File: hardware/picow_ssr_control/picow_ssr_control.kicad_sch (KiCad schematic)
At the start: 6 parts

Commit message: Updated schemas
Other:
- sheet Pico W Control ports: added none; removed VBUS, VSYS
- sheet Power Management ports: added none; removed VBUS, VSYS
- note added: "Pico W SSR Control"
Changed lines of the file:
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@@
   (title_block
     (title "Picow SSR Control")
-    (date "2023-01-27")
+    (date "2023-01-28")
     (rev "0.0.10")
     (comment 2 "http://creativecommons.org/licenses/by-sa/4.0/")
@@
     (comment 6 "Hardware License: CERN-OHL-W")
   )
-  (junction (at 127 55.88) (diameter 0) (color 255 255 0 1)
+  (junction (at 111.76 40.64) (diameter 0) (color 255 255 0 1)
   )
   (junction (at 27.94 152.4) (diameter 0) (color 0 0 0 0)
@@
   (junction (at 27.94 157.48) (diameter 0) (color 0 0 0 0)
   )
-  (junction (at 132.08 71.12) (diameter 0) (color 255 255 0 1)
+  (junction (at 116.84 55.88) (diameter 0) (color 255 255 0 1)
   )
   (polyline (pts (xy 17.78 172.72) (xy 17.78 195.58))
@@
     (stroke (width 0) (type default) (color 0 0 0 0))
   )
-  (bus (pts (xy 127 55.88) (xy 127 106.68))
+  (bus (pts (xy 111.76 40.64) (xy 111.76 81.28))
     (stroke (width 0) (type default) (color 255 255 0 1))
   )
@@
     (stroke (width 0) (type default) (color 0 0 0 0))
   )
-  (bus (pts (xy 132.08 71.12) (xy 152.4 71.12))
+  (bus (pts (xy 116.84 55.88) (xy 132.08 55.88))
     (stroke (width 0) (type default) (color 255 255 0 1))
   )
@@
     (stroke (width 0) (type default) (color 0 0 0 0))
   )
-  (bus (pts (xy 127 55.88) (xy 152.4 55.88))
+  (bus (pts (xy 111.76 40.64) (xy 132.08 40.64))
     (stroke (width 0) (type default) (color 255 255 0 1))
   )
@@
     (stroke (width 0) (type default) (color 0 0 0 0))
   )
-  (bus (pts (xy 132.08 114.3) (xy 114.3 114.3))
+  (bus (pts (xy 116.84 88.9) (xy 99.06 88.9))
     (stroke (width 0) (type default) (color 255 255 0 1))
   )
@@
     (stroke (width 0) (type default) (color 0 0 0 0))
   )
-  (wire (pts (xy 45.72 55.88) (xy 76.2 55.88))
-    (stroke (width 0) (type default) (color 0 0 0 0))
-  )
   (wire (pts (xy 27.94 152.4) (xy 27.94 157.48))
     (stroke (width 0) (type default) (color 0 0 0 0))
   )
-  (bus (pts (xy 114.3 106.68) (xy 127 106.68))
+  (bus (pts (xy 99.06 81.28) (xy 111.76 81.28))
     (stroke (width 0) (type default) (color 255 255 0 1))
   )
@@
     (stroke (width 0) (type default) (color 0 0 0 0))
   )
-  (bus (pts (xy 132.08 71.12) (xy 132.08 114.3))
+  (bus (pts (xy 116.84 55.88) (xy 116.84 88.9))
     (stroke (width 0) (type default) (color 255 255 0 1))
   )
-  (bus (pts (xy 114.3 71.12) (xy 132.08 71.12))
+  (bus (pts (xy 99.06 55.88) (xy 116.84 55.88))
     (stroke (width 0) (type default) (color 255 255 0 1))
   )
-  (wire (pts (xy 45.72 60.96) (xy 76.2 60.96))
-    (stroke (width 0) (type default) (color 0 0 194 1))
-  )
-  (bus (pts (xy 114.3 55.88) (xy 127 55.88))
+  (bus (pts (xy 99.06 40.64) (xy 111.76 40.64))
     (stroke (width 0) (type default) (color 255 255 0 1))
   )
@@
     )
   )
+  (text "Pico W SSR Control" (at 15.24 20.32 0)
+    (effects (font (size 4 4) bold) (justify left bottom))
+  )
   (text "Mounting Holes" (at 20.32 142.24 0)
     (effects (font (size 2 2) (thickness 0.4) bold) (justify left bottom))
@@
     )
   )
-  (sheet (at 76.2 101.6) (size 38.1 17.78) (fields_autoplaced)
+  (sheet (at 60.96 76.2) (size 38.1 17.78) (fields_autoplaced)
     (stroke (width 0.1524) (type solid) (color 0 0 0 0))
     (fill (color 0 0 0 0.0000))
-    (property "Sheet name" "Manual Control" (id 0) (at 76.2 100.5234 0)
+    (property "Sheet name" "Manual Control" (id 0) (at 60.96 75.1234 0)
       (effects (font (size 2 2) bold) (justify left bottom))
     )
-    (property "Sheet file" "manual_control.kicad_sch" (id 1) (at 76.2 119.9646 0)
+    (property "Sheet file" "manual_control.kicad_sch" (id 1) (at 60.96 94.5646 0)
       (effects (font (size 1.27 1.27)) (justify left top))
     )
-    (pin "BANK_A{CNTL[1..4]}" passive (at 114.3 106.68 0)
+    (pin "BANK_A{CNTL[1..4]}" passive (at 99.06 81.28 0)
       (effects (font (size 1.27 1.27)) (justify right))
     )
-    (pin "BANK_B{CNTL[5..8]}" passive (at 114.3 114.3 0)
+    (pin "BANK_B{CNTL[5..8]}" passive (at 99.06 88.9 0)
       (effects (font (size 1.27 1.27)) (justify right))
     )
   )
-  (sheet (at 152.4 50.8) (size 38.1 25.4) (fields_autoplaced)
+  (sheet (at 132.08 35.56) (size 38.1 25.4) (fields_autoplaced)
     (stroke (width 0.1524) (type solid) (color 0 0 0 0))
     (fill (color 0 0 0 0.0000))
-    (property "Sheet name" "Control Out" (id 0) (at 152.4 49.7234 0)
+    (property "Sheet name" "Control Out" (id 0) (at 132.08 34.4834 0)
       (effects (font (size 2 2) bold) (justify left bottom))
     )
-    (property "Sheet file" "control_out.kicad_sch" (id 1) (at 152.4 76.7846 0)
+    (property "Sheet file" "control_out.kicad_sch" (id 1) (at 132.08 61.5446 0)
       (effects (font (size 1.27 1.27)) (justify left top))
     )
-    (pin "BANK_B{CNTL[5..8]}" input (at 152.4 71.12 180)
+    (pin "BANK_B{CNTL[5..8]}" input (at 132.08 55.88 180)
       (effects (font (size 1.27 1.27)) (justify left))
     )
-    (pin "BANK_A{CNTL[1..4]}" input (at 152.4 55.88 180)
+    (pin "BANK_A{CNTL[1..4]}" input (at 132.08 40.64 180)
       (effects (font (size 1.27 1.27)) (justify left))
     )
   )
-  (sheet (at 15.24 50.8) (size 30.48 17.78)
+  (sheet (at 15.24 35.56) (size 30.48 17.78)
     (stroke (width 0.1524) (type solid) (color 0 0 0 0))
     (fill (color 0 0 0 0.0000))
-    (property "Sheet name" "Power Management" (id 0) (at 15.21 49.73 0)
+    (property "Sheet name" "Power Management" (id 0) (at 15.21 34.49 0)
       (effects (font (size 2 2) bold) (justify left bottom))
     )
-    (property "Sheet file" "power_in.kicad_sch" (id 1) (at 15.24 65.3546 0)
+    (property "Sheet file" "power_in.kicad_sch" (id 1) (at 15.24 54.102 0)
       (effects (font (size 1.27 1.27)) (justify left top))
     )
-    (pin "VBUS" input (at 45.72 60.96 0)
-      (effects (font (size 1.27 1.27)) (justify right))
-    )
-    (pin "VSYS" output (at 45.72 55.88 0)
-      (effects (font (size 1.27 1.27)) (justify right))
-    )
-  )
-  (sheet (at 76.2 50.8) (size 38.1 25.4) (fields_autoplaced)
+  )
+  (sheet (at 60.96 35.56) (size 38.1 25.4) (fields_autoplaced)
     (stroke (width 0.1524) (type solid) (color 0 0 0 0))
     (fill (color 0 0 0 0.0000))
-    (property "Sheet name" "Pico W Control" (id 0) (at 76.2 49.7234 0)
+    (property "Sheet name" "Pico W Control" (id 0) (at 60.96 34.4834 0)
       (effects (font (size 2 2) bold) (justify left bottom))
     )
-    (property "Sheet file" "picow_control.kicad_sch" (id 1) (at 76.2 76.7846 0)
+    (property "Sheet file" "picow_control.kicad_sch" (id 1) (at 60.96 61.5446 0)
       (effects (font (size 1.27 1.27)) (justify left top))
     )
-    (pin "VSYS" input (at 76.2 55.88 180)
-      (effects (font (size 1.27 1.27)) (justify left))
-    )
-    (pin "VBUS" output (at 76.2 60.96 180)
-      (effects (font (size 1.27 1.27)) (justify left))
-    )
-    (pin "BANK_B{CNTL[5..8]}" output (at 114.3 71.12 0)
+    (pin "BANK_B{CNTL[5..8]}" output (at 99.06 55.88 0)
       (effects (font (size 1.27 1.27)) (justify right))
     )
-    (pin "BANK_A{CNTL[1..4]}" output (at 114.3 55.88 0)
+    (pin "BANK_A{CNTL[1..4]}" output (at 99.06 40.64 0)
       (effects (font (size 1.27 1.27)) (justify right))
     )
@@
       (reference "#PWR02") (unit 1) (value "GNDPWR") (footprint "")
     )
-    (path "/a7cfd456-3e8b-4e3a-9dc2-46f9e2f2d504/629605ae-093c-4e6d-899a-88d1584af921"
-      (reference "#PWR03") (unit 1) (value "+VDC") (footprint "")
+    (path "/e73b6763-033f-46e1-9aa1-1a9dd8951104/9b96088d-8927-4eed-a676-8c97a42df7c3"
+      (reference "#PWR03") (unit 1) (value "+5V") (footprint "")
     )
     (path "/a7cfd456-3e8b-4e3a-9dc2-46f9e2f2d504/e82ef186-d0ca-4236-82f0-31dacbf8334b"
@@
       (reference "#PWR08") (unit 1) (value "GNDPWR") (footprint "")
     )
+    (path "/e73b6763-033f-46e1-9aa1-1a9dd8951104/a1f016ef-c56d-4024-a5c2-bbf8628338e8"
+      (reference "#PWR09") (unit 1) (value "GNDPWR") (footprint "")
+    )
     (path "/9a31bd8a-9f6c-42a4-99bd-41703d57702f/772ba637-5c96-463c-a7e9-f497978fe28b"
       (reference "#PWR011") (unit 1) (value "GNDPWR") (footprint "")
@@
       (reference "C2") (unit 1) (value "100n") (footprint "Capacitor_SMD:C_0805_2012Metric")
     )
+    (path "/e73b6763-033f-46e1-9aa1-1a9dd8951104/bbf39d05-6c1b-4fb4-8b43-6cae4cd26d1a"
+      (reference "C3") (unit 1) (value "100n") (footprint "Capacitor_SMD:C_0805_2012Metric")
+    )
     (path "/f53b3346-3cf3-4e8a-a8f1-2752a8de3dda"
       (reference "FID1") (unit 1) (value "Fiducial") (footprint "Fiducial:Fiducial_0.5mm_Mask1mm")
@@
       (reference "Q1") (unit 1) (value "IRF4905PBF") (footprint "dragon_mobile:TO254P469X1042X1967-3P")
     )
-    (path "/a7cfd456-3e8b-4e3a-9dc2-46f9e2f2d504/0aaa2676-a0f6-441f-b4d2-d7dc39aa23a7"
-      (reference "Q2") (unit 1) (value "DMG2301L") (footprint "Package_TO_SOT_SMD:SOT-23")
+    (path "/e73b6763-033f-46e1-9aa1-1a9dd8951104/eebbe18a-7277-4977-b24b-8f1e8d50465e"
+      (reference "Q2") (unit 1) (value "DMG2305UX-7") (footprint "Package_TO_SOT_SMD:SOT-23")
     )
     (path "/e73b6763-033f-46e1-9aa1-1a9dd8951104/d899e107-a7e2-42d6-b04f-38deada1b33f"
@@
     )
     (path "/a7cfd456-3e8b-4e3a-9dc2-46f9e2f2d504/ad138bad-9bd6-4294-a36b-690f0cb15cb6"
-      (reference "REG1") (unit 1) (value "LM7805") (footprint "SOT230P700X180-4N")
+      (reference "REG1") (unit 1) (value "LM7805") (footprint "Package_TO_SOT_SMD:SOT-223")
     )
     (path "/a7cfd456-3e8b-4e3a-9dc2-46f9e2f2d504/09d3304d-431b-4b30-adf2-e3fc27b505b4"
@@
     )
     (path "/a7cfd456-3e8b-4e3a-9dc2-46f9e2f2d504/102251af-7d71-4271-be1e-7c08e53df276"
-      (reference "RZ1") (unit 1) (value "100k") (footprint "Resistor_SMD:R_0805_2012Metric")
+      (reference "RZ1") (unit 1) (value "100k") (footprint "Resistor_SMD:R_0603_1608Metric")
     )
     (path "/6f32e7f5-0a22-4bb9-a836-1e48dd69b48f/8f786c38-4138-4f6b-b98d-ec240583ea11"

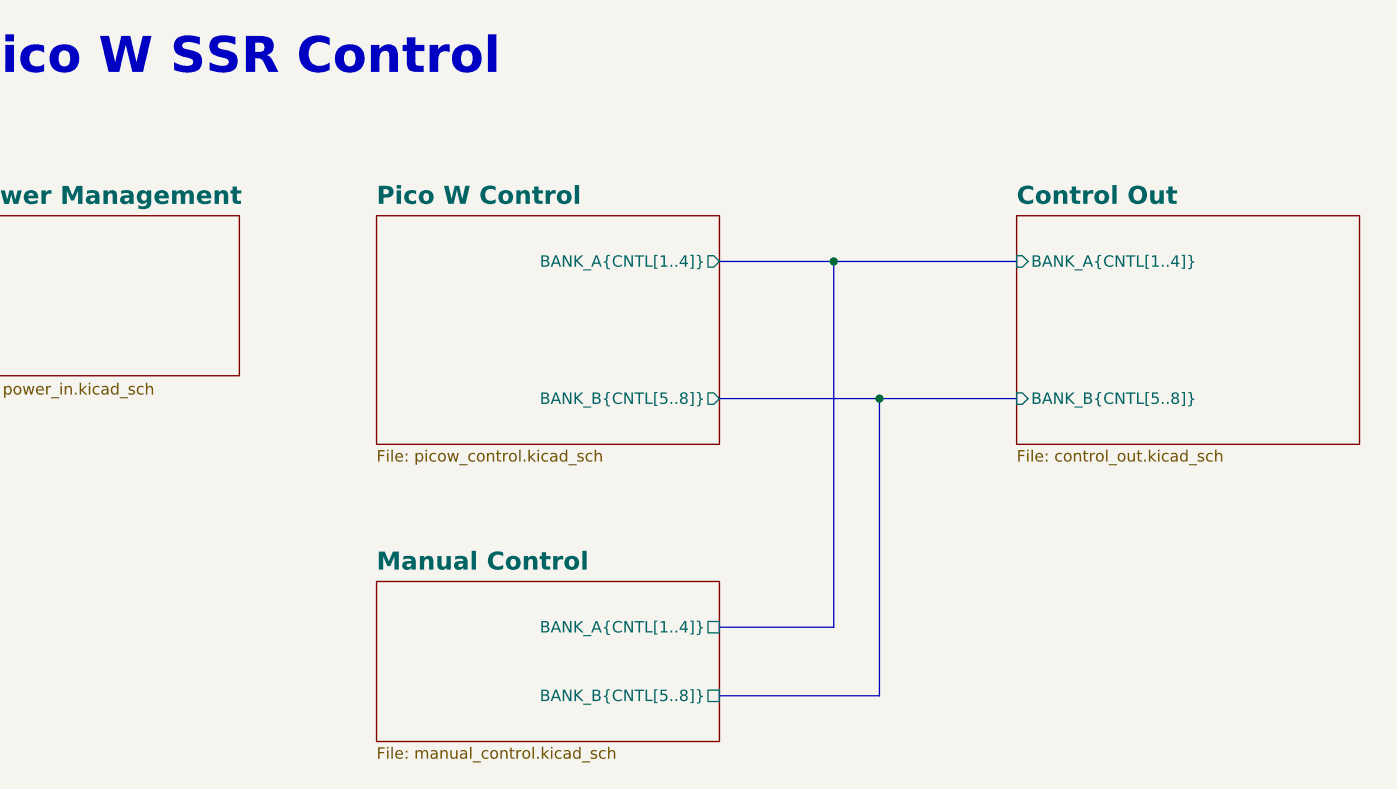
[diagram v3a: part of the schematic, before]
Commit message: Power supply changes plus misc.
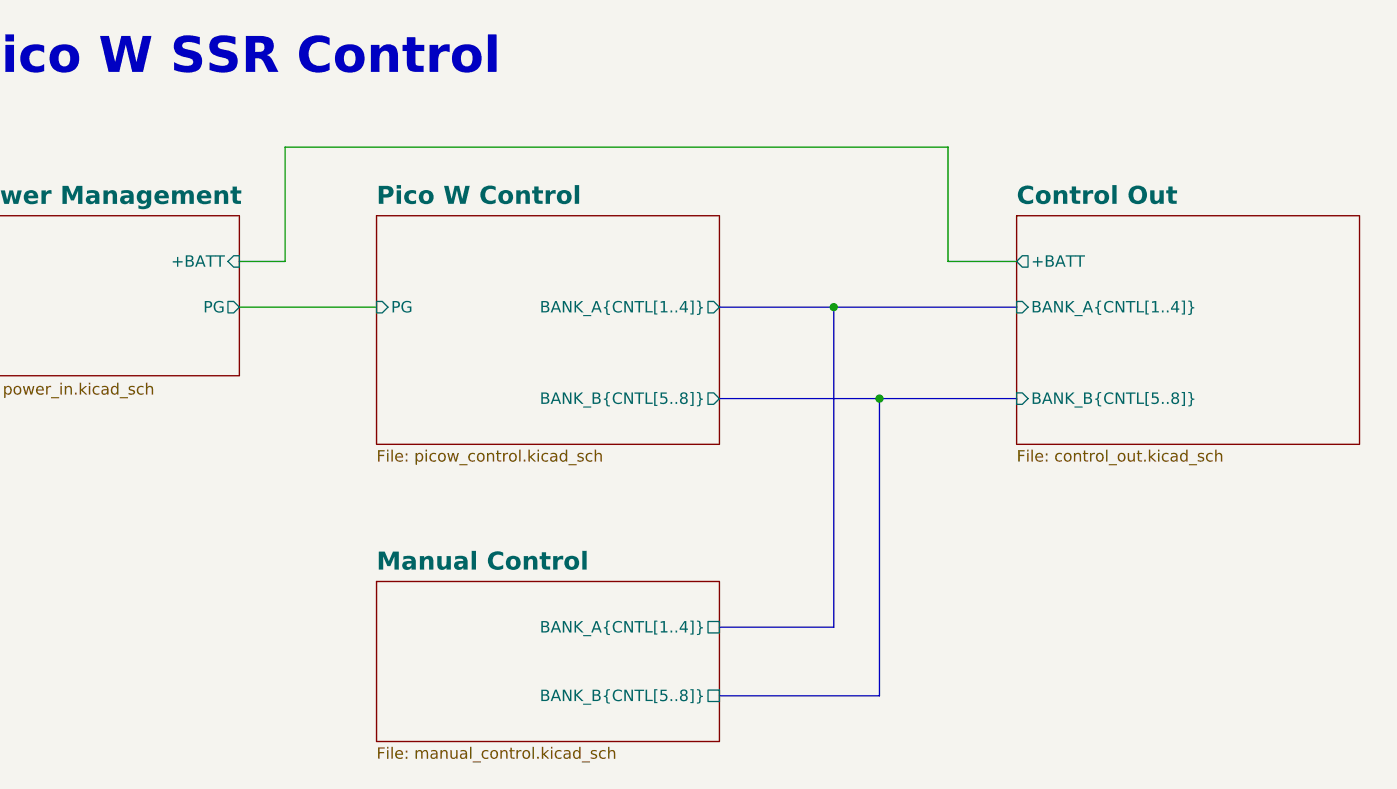
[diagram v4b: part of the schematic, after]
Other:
- sheet Control Out ports: added +BATT; removed none
- sheet Pico W Control ports: added PG; removed none
- sheet Power Management ports: added +BATT, PG; removed none

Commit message: Pre KiCad 7.0.0 WIP
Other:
- sheet Control Out ports: added BANK_A{OUT[1..4]}, BANK_B{OUT[5..8]}; removed BANK_A{CNTL[1..4]}, BANK_B{CNTL[5..8]}
- sheet Manual Control ports: added BANK_A{OUT[1..4]}, BANK_B{OUT[5..8]}; removed BANK_A{CNTL[1..4]}, BANK_B{CNTL[5..8]}
- sheet Pico W Control ports: added BANK_A{OUT[1..4]}, BANK_B{OUT[5..8]}; removed BANK_A{CNTL[1..4]}, BANK_B{CNTL[5..8]}
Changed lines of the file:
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@@
       (effects (font (size 1.27 1.27)) (justify left top))
     )
-    (pin "BANK_A{CNTL[1..4]}" passive (at 99.06 81.28 0)
-      (effects (font (size 1.27 1.27)) (justify right))
-    )
-    (pin "BANK_B{CNTL[5..8]}" passive (at 99.06 88.9 0)
+    (pin "BANK_A{OUT[1..4]}" passive (at 99.06 81.28 0)
+      (effects (font (size 1.27 1.27)) (justify right))
+    )
+    (pin "BANK_B{OUT[5..8]}" passive (at 99.06 88.9 0)
       (effects (font (size 1.27 1.27)) (justify right))
     )
@@
       (effects (font (size 1.27 1.27)) (justify left top))
     )
-    (pin "BANK_B{CNTL[5..8]}" input (at 132.08 55.88 180)
-      (effects (font (size 1.27 1.27)) (justify left))
-    )
-    (pin "BANK_A{CNTL[1..4]}" input (at 132.08 45.72 180)
+    (pin "BANK_B{OUT[5..8]}" input (at 132.08 55.88 180)
+      (effects (font (size 1.27 1.27)) (justify left))
+    )
+    (pin "BANK_A{OUT[1..4]}" input (at 132.08 45.72 180)
       (effects (font (size 1.27 1.27)) (justify left))
     )
@@
       (effects (font (size 1.27 1.27)) (justify left top))
     )
-    (pin "BANK_B{CNTL[5..8]}" output (at 99.06 55.88 0)
-      (effects (font (size 1.27 1.27)) (justify right))
-    )
-    (pin "BANK_A{CNTL[1..4]}" output (at 99.06 45.72 0)
+    (pin "BANK_B{OUT[5..8]}" output (at 99.06 55.88 0)
+      (effects (font (size 1.27 1.27)) (justify right))
+    )
+    (pin "BANK_A{OUT[1..4]}" output (at 99.06 45.72 0)
       (effects (font (size 1.27 1.27)) (justify right))
     )
@@
     )
     (path "/e73b6763-033f-46e1-9aa1-1a9dd8951104/d899e107-a7e2-42d6-b04f-38deada1b33f"
-      (reference "QD1") (unit 1) (value "2N7002K") (footprint "Package_TO_SOT_SMD:SOT-23")
+      (reference "QD1") (unit 1) (value "2N7002K") (footprint "dragon_mobile:2V7002KT1G")
     )
     (path "/e73b6763-033f-46e1-9aa1-1a9dd8951104/521664a9-1b24-4eef-ad16-961e053a1aa1"
-      (reference "QD2") (unit 1) (value "2N7002K") (footprint "Package_TO_SOT_SMD:SOT-23")
+      (reference "QD2") (unit 1) (value "2N7002K") (footprint "dragon_mobile:2V7002KT1G")
     )
     (path "/e73b6763-033f-46e1-9aa1-1a9dd8951104/6f8e193b-fc7f-4c0f-b90c-fd3fe530eeda"
-      (reference "QD3") (unit 1) (value "2N7002K") (footprint "Package_TO_SOT_SMD:SOT-23")
+      (reference "QD3") (unit 1) (value "2N7002K") (footprint "dragon_mobile:2V7002KT1G")
     )
     (path "/e73b6763-033f-46e1-9aa1-1a9dd8951104/49c8d0a3-40d2-4ffc-ba19-718f8b19dd8f"
-      (reference "QD4") (unit 1) (value "2N7002K") (footprint "Package_TO_SOT_SMD:SOT-23")
+      (reference "QD4") (unit 1) (value "2N7002K") (footprint "dragon_mobile:2V7002KT1G")
     )
     (path "/e73b6763-033f-46e1-9aa1-1a9dd8951104/e15f8dc6-949b-4e5e-9970-bffb8388feef"
-      (reference "QD5") (unit 1) (value "2N7002K") (footprint "Package_TO_SOT_SMD:SOT-23")
+      (reference "QD5") (unit 1) (value "2N7002K") (footprint "dragon_mobile:2V7002KT1G")
     )
     (path "/e73b6763-033f-46e1-9aa1-1a9dd8951104/b796601d-2fa5-485d-a31f-9ee7539aa87e"
-      (reference "QD6") (unit 1) (value "2N7002K") (footprint "Package_TO_SOT_SMD:SOT-23")
+      (reference "QD6") (unit 1) (value "2N7002K") (footprint "dragon_mobile:2V7002KT1G")
     )
     (path "/e73b6763-033f-46e1-9aa1-1a9dd8951104/abe5ca34-fc23-4eae-87f7-095b59f38aca"
-      (reference "QD7") (unit 1) (value "2N7002K") (footprint "Package_TO_SOT_SMD:SOT-23")
+      (reference "QD7") (unit 1) (value "2N7002K") (footprint "dragon_mobile:2V7002KT1G")
     )
     (path "/e73b6763-033f-46e1-9aa1-1a9dd8951104/5e4296ad-2232-41cc-8231-355570914aab"
-      (reference "QD8") (unit 1) (value "2N7002K") (footprint "Package_TO_SOT_SMD:SOT-23")
+      (reference "QD8") (unit 1) (value "2N7002K") (footprint "dragon_mobile:2V7002KT1G")
     )
     (path "/a7cfd456-3e8b-4e3a-9dc2-46f9e2f2d504/a0c350aa-6202-4c5e-a23d-79f61209dccb"
